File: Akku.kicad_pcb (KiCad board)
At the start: 2 copper layers, 100 x 160 mm, 46 parts, among them J1 +/- Stecker, J2 load/up, J3 down/en/clear, P7 CONN_02X10, P8 CONN_02X10, P9 CONN_02X10, SW1 UP_Bonsai_SWITCH_INV, SW2 DOWN_Bonsai_SWITCH_INV, SW3 CLR_Bonsai_SWITCH_INV, U1 74HC14, U2 7400, U4 7408, U5 74LS193, U6 74LS541, U7 74LS193, U8 74LS540

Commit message: akku and wireing in pcb
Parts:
- moved D3 74.6 mm to (117.5, 170.8)
- moved D1 65.1 mm to (63.5, 119.4), turned to 180 degrees
- moved U5 34.9 mm to (107.3, 171.4)
- moved U7 13.4 mm to (83.2, 171.4)
- moved D4 12.7 mm to (94.0, 121.9)
- moved R13 12.7 mm to (94.0, 124.5)
- moved D5 11.4 mm to (99.1, 121.9)
- moved R15 11.4 mm to (99.1, 124.7)
- moved D2 10.9 mm to (114.9, 177.8)
- moved U8 10.2 mm to (99.1, 149.9)
- moved D6 10.2 mm to (104.1, 121.9)
- moved R16 10.2 mm to (104.1, 124.7)
- moved D8 8.89 mm to (109.2, 121.9)
- moved R17 8.89 mm to (109.2, 124.7)
- moved D9 7.62 mm to (114.3, 121.9)
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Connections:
- SW3 pad 6: (no net) -> GND
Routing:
- net GND: track 255.3 -> 592.3 mm, vias 2 -> 8
- net Net-(U1-Pad4): track 2.54 -> 209.1 mm
- net VCC: track 595.8 -> 780.3 mm, vias 0 -> 4
- net Net-(D7-Pad2): track 0.00 -> 144.8 mm
- net Net-(D1-Pad2): track 0.00 -> 122.4 mm
- net CLR: track 27.2 -> 125.1 mm, vias 0 -> 3
- net Net-(U1-Pad11): track 0.00 -> 95.3 mm, vias 0 -> 1
- net Net-(U1-Pad13): track 28.6 -> 107.7 mm, vias 0 -> 1
- net RPB4: track 45.9 -> 116.1 mm, vias 0 -> 4
- net RPB3: track 21.9 -> 82.8 mm, vias 0 -> 2
- net Net-(D2-Pad2): track 0.00 -> 30.6 mm
- net Net-(D3-Pad2): track 0.00 -> 26.3 mm
- net Net-(R12-Pad2): track 14.4 -> 21.4 mm
- net ^enable: track 108.0 -> 111.0 mm
- net Net-(R9-Pad2): track 17.4 -> 20.0 mm
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
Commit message: Akku pc finished
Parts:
- added C1: C, tg_foodprint:C_Disc_D10.0mm_W2.5mm_P5.00mm, F.Cu at (86.4, 172.7)
- added C2: C, tg_foodprint:C_Disc_D10.0mm_W2.5mm_P5.00mm, F.Cu at (66.7, 208.9)
- added C3: C, tg_foodprint:C_Disc_D10.0mm_W2.5mm_P5.00mm, F.Cu at (94.0, 149.9)
- added D13: D, Pin_Headers:D_DO-41_SOD81_P10.16mm_Horizontal, F.Cu at (63.5, 87.6)
- moved U7 24.3 mm to (107.4, 171.4)
- moved U5 24.1 mm to (83.2, 171.3)
- moved P7 1.27 mm to (48.3, 113.0)
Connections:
- U5 pad 12: Net-(U5-Pad12) -> (no net)
- U5 pad 13: Net-(U5-Pad13) -> (no net)
- U5 pad 4: Net-(U1-Pad13) -> Net-(U5-Pad4)
- U5 pad 5: Net-(U1-Pad11) -> Net-(U5-Pad5)
- U7 pad 12: (no net) -> Net-(U5-Pad5)
- U7 pad 13: (no net) -> Net-(U5-Pad4)
- U7 pad 4: Net-(U5-Pad13) -> Net-(U1-Pad13)
- U7 pad 5: Net-(U5-Pad12) -> Net-(U1-Pad11)
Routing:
- net /a7: track 0.00 -> 303.7 mm, vias 0 -> 4
- net /a6: track 0.00 -> 302.3 mm, vias 0 -> 6
- net /a5: track 0.00 -> 272.5 mm, vias 0 -> 6
- net /a2: track 0.00 -> 268.1 mm, vias 0 -> 6
- net /a4: track 0.00 -> 262.0 mm, vias 0 -> 6
- net /a3: track 0.00 -> 246.2 mm, vias 0 -> 6
- net /a1: track 0.00 -> 215.7 mm, vias 0 -> 6
- net /a0: track 0.00 -> 204.4 mm, vias 0 -> 4
- net Net-(U6-Pad8): track 0.00 -> 80.4 mm, vias 0 -> 2
- net Net-(U6-Pad6): track 0.00 -> 69.9 mm, vias 0 -> 2
- net Net-(U6-Pad7): track 0.00 -> 69.9 mm, vias 0 -> 2
- net Net-(U5-Pad3): track 0.00 -> 67.8 mm, vias 0 -> 2
- net Net-(U6-Pad9): track 0.00 -> 66.9 mm
- net Net-(U5-Pad2): track 0.00 -> 61.1 mm, vias 0 -> 2
- net GND: track 592.3 -> 652.5 mm, vias 8 -> 11
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
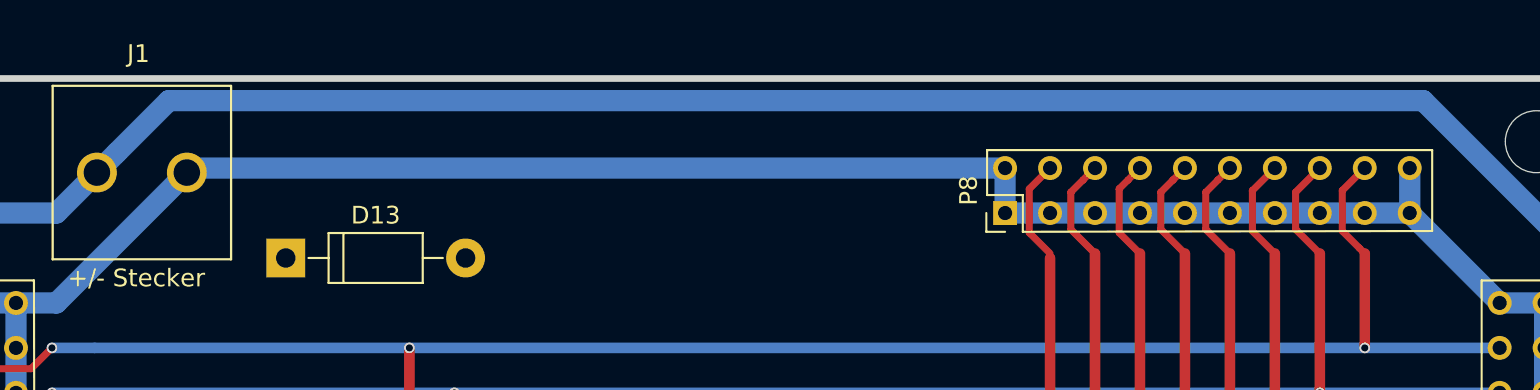
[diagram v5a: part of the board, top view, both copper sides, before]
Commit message: Eintakt libs fixed
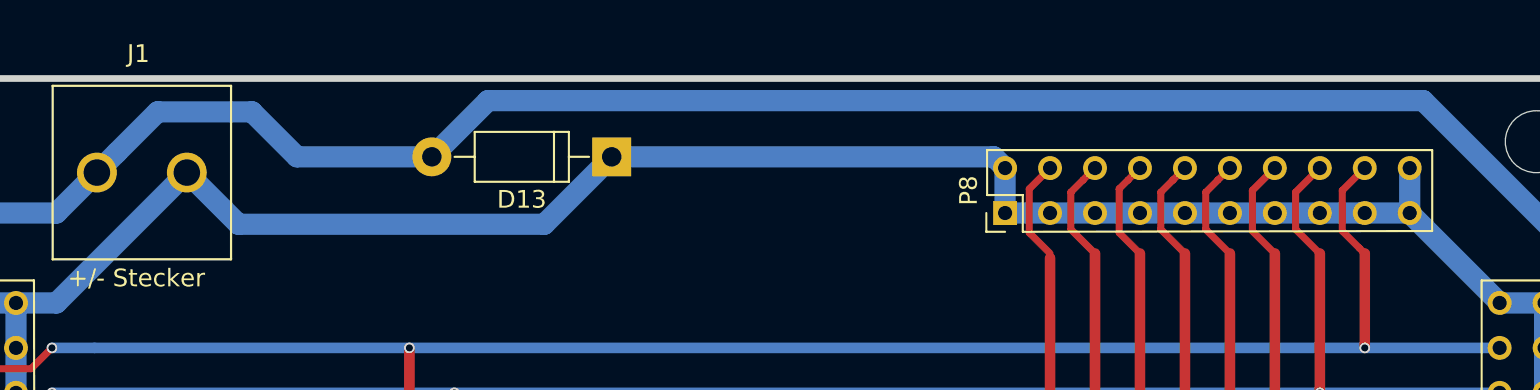
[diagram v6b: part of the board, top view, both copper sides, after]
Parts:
- moved D13 19.3 mm to (81.9, 81.9), turned to 180 degrees
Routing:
- net GND: track 652.5 -> 655.5 mm
- net VCC: track 785.1 -> 787.2 mm
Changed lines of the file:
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@@
     (thickness 1.6)
     (drawings 3)
-    (tracks 850)
+    (tracks 857)
     (zones 0)
     (modules 50)
@@
     (visible_elements FFFFFF7F)
     (pcbplotparams
-      (layerselection 0x00030_80000001)
+      (layerselection 0x00030_ffffffff)
       (usegerberextensions false)
       (usegerberattributes false)
       (usegerberadvancedattributes false)
       (creategerberjobfile false)
-      (excludeedgelayer true)
+      (excludeedgelayer false)
       (linewidth 0.100000)
       (plotframeref false)
@@
       (padsonsilk false)
       (subtractmaskfromsilk false)
-      (outputformat 1)
+      (outputformat 4)
       (mirror false)
-      (drillshape 1)
+      (drillshape 0)
       (scaleselection 1)
       (outputdirectory ""))
@@
   )
   (module Pin_Headers:D_DO-41_SOD81_P10.16mm_Horizontal (layer F.Cu)
-    (at 63.5 87.63)
+    (at 81.915 81.915 180)
     (descr "D, DO-41_SOD81 series, Axial, Horizontal, pin pitch=10.16mm, , length*diameter=5.2*2.7mm^2, , http://www.diodes.com/_files/packages/DO-41%20(Plastic).pdf")
     (tags "D DO-41_SOD81 series Axial Horizontal pin pitch 10.16mm  length 5.2mm diameter 2.7mm")
-    (fp_text reference D13 (at 5.08 -2.41) (layer F.SilkS)
-      (effects (font (size 1 1) (thickness 0.15)))
-    )
-    (fp_text value D (at 5.08 2.41) (layer F.Fab)
+    (fp_text reference D13 (at 5.08 -2.41 180) (layer F.SilkS)
+      (effects (font (size 1 1) (thickness 0.15)))
+    )
+    (fp_text value D (at 5.08 2.41 180) (layer F.Fab)
       (effects (font (size 1 1) (thickness 0.15)))
     )
@@
     (fp_line (start 2.48 1.35) (end 7.68 1.35) (layer F.Fab) (width 0.1))
     (fp_line (start 2.48 -1.35) (end 2.48 1.35) (layer F.Fab) (width 0.1))
-    (fp_text user %R (at 5.08 0) (layer F.Fab)
-      (effects (font (size 1 1) (thickness 0.15)))
-    )
-    (pad 2 thru_hole oval (at 10.16 0) (size 2.2 2.2) (drill 1.1) (layers *.Cu *.Mask)
+    (fp_text user %R (at 5.08 0 180) (layer F.Fab)
+      (effects (font (size 1 1) (thickness 0.15)))
+    )
+    (pad 2 thru_hole oval (at 10.16 0 180) (size 2.2 2.2) (drill 1.1) (layers *.Cu *.Mask)
       (net 2 VCC))
-    (pad 1 thru_hole rect (at 0 0) (size 2.2 2.2) (drill 1.1) (layers *.Cu *.Mask)
+    (pad 1 thru_hole rect (at 0 0 180) (size 2.2 2.2) (drill 1.1) (layers *.Cu *.Mask)
       (net 10 GND))
     (model ${KISYS3DMOD}/Diodes_THT.3dshapes/D_DO-41_SOD81_P10.16mm_Horizontal.wrl
@@
   (segment (start 82.55 224.155) (end 82.55 219.075) (width 1.2) (layer B.Cu) (net 2))
   (segment (start 83.82 206.745823) (end 83.82 205.74) (width 0.6) (layer B.Cu) (net 2))
-  (segment (start 53.956999 81.679001) (end 52.832 82.804) (width 1.2) (layer B.Cu) (net 2) (status 20))
-  (segment (start 138.60999 89.589992) (end 127.759998 78.74) (width 1.2) (layer B.Cu) (net 2))
-  (segment (start 127.759998 78.74) (end 56.896 78.74) (width 1.2) (layer B.Cu) (net 2))
   (segment (start 82.55 231.14) (end 100.33 231.14) (width 1.2) (layer B.Cu) (net 2))
   (segment (start 105.41 236.22) (end 127 236.22) (width 1.2) (layer B.Cu) (net 2))
   (segment (start 137.130001 231.169999) (end 138.60999 229.69001) (width 1.2) (layer B.Cu) (net 2))
   (segment (start 127 236.22) (end 132.050001 231.169999) (width 1.2) (layer B.Cu) (net 2))
-  (segment (start 56.896 78.74) (end 53.956999 81.679001) (width 1.2) (layer B.Cu) (net 2))
   (segment (start 100.33 231.14) (end 105.41 236.22) (width 1.2) (layer B.Cu) (net 2))
   (segment (start 132.050001 231.169999) (end 137.130001 231.169999) (width 1.2) (layer B.Cu) (net 2))
@@
   (segment (start 52.832 82.804) (end 50.546 85.09) (width 1.2) (layer B.Cu) (net 2) (status 10))
   (segment (start 138.60999 119.38) (end 93.98 119.38) (width 1.2) (layer B.Cu) (net 2) (status 20))
-  (segment (start 138.60999 119.38) (end 138.60999 89.589992) (width 1.2) (layer B.Cu) (net 2))
   (segment (start 138.60999 229.69001) (end 138.60999 119.38) (width 1.2) (layer B.Cu) (net 2))
   (segment (start 66.675 144.78) (end 65.405 143.51) (width 1.2) (layer B.Cu) (net 2))
@@
   (segment (start 69.135 203.915) (end 69.85 203.2) (width 1.2) (layer B.Cu) (net 2))
   (segment (start 66.675 203.915) (end 69.135 203.915) (width 1.2) (layer B.Cu) (net 2))
+  (segment (start 53.956999 81.679001) (end 52.832 82.804) (width 1.2) (layer B.Cu) (net 2))
+  (segment (start 61.595 79.375) (end 56.261 79.375) (width 1.2) (layer B.Cu) (net 2))
+  (segment (start 138.60999 89.589992) (end 127.759998 78.74) (width 1.2) (layer B.Cu) (net 2))
+  (segment (start 127.759998 78.74) (end 74.93 78.74) (width 1.2) (layer B.Cu) (net 2))
+  (segment (start 74.93 78.74) (end 71.755 81.915) (width 1.2) (layer B.Cu) (net 2))
+  (segment (start 138.60999 119.38) (end 138.60999 89.589992) (width 1.2) (layer B.Cu) (net 2))
+  (segment (start 71.755 81.915) (end 64.135 81.915) (width 1.2) (layer B.Cu) (net 2))
+  (segment (start 56.261 79.375) (end 53.956999 81.679001) (width 1.2) (layer B.Cu) (net 2))
+  (segment (start 64.135 81.915) (end 61.595 79.375) (width 1.2) (layer B.Cu) (net 2))
   (segment (start 99.06 121.92) (end 99.06 124.714) (width 0.6) (layer B.Cu) (net 3) (status 30))
   (segment (start 104.14 124.714) (end 104.14 121.92) (width 0.6) (layer B.Cu) (net 4) (status 30))
@@
   (segment (start 48.006 228.346) (end 43.18 223.52) (width 1.2) (layer B.Cu) (net 10))
   (segment (start 64.77 228.346) (end 58.42 228.346) (width 1.2) (layer B.Cu) (net 10) (status 30))
-  (segment (start 58.166 82.55) (end 57.912 82.804) (width 1.2) (layer B.Cu) (net 10) (status 30))
-  (segment (start 104.14 82.55) (end 58.166 82.55) (width 1.2) (layer B.Cu) (net 10) (status 30))
   (segment (start 104.14 82.55) (end 104.14 85.09) (width 1.2) (layer B.Cu) (net 10) (status 30))
   (segment (start 124.251002 85.09) (end 127 85.09) (width 1.2) (layer B.Cu) (net 10) (status 30))
@@
   (segment (start 64.77 210.82) (end 66.675 208.915) (width 1.2) (layer B.Cu) (net 10))
   (segment (start 63.5 210.82) (end 64.77 210.82) (width 1.2) (layer B.Cu) (net 10))
+  (segment (start 78.105 85.725) (end 60.833 85.725) (width 1.2) (layer B.Cu) (net 10))
+  (segment (start 81.915 81.915) (end 78.105 85.725) (width 1.2) (layer B.Cu) (net 10))
+  (segment (start 104.14 82.55) (end 103.505 81.915) (width 1.2) (layer B.Cu) (net 10))
+  (segment (start 60.833 85.725) (end 57.912 82.804) (width 1.2) (layer B.Cu) (net 10))
+  (segment (start 103.505 81.915) (end 81.915 81.915) (width 1.2) (layer B.Cu) (net 10))
   (segment (start 96.52 203.2) (end 96.52 200.66) (width 1.2) (layer B.Cu) (net 11) (status 30))
   (segment (start 46.355 133.985) (end 60.96 119.38) (width 0.6) (layer B.Cu) (net 12) (status 20))

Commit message: BIB Cleanup finished
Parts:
- C1, C2, C3: footprint tg_foodprint:C_Disc_D10.0mm_W2.5mm_P5.00mm -> allBonsaiFootprintsLibs:C_Disc_D10.0mm_W2.5mm_P5.00mm
- P7, P8, P9: footprint tg_foodprint:Pin_Header_Straight_2x10_Pitch2.00mmBonsai.pretty -> allBonsaiFootprintsLibs:Pin_Header_Straight_2x10_Pitch2.00mmBonsai.pretty
- REF**: footprint tg_foodprint:EuroBoard160mmX100mm_holes -> allBonsaiFootprintsLibs:EuroBoard160mmX100mm_holes
- SW1, SW2, SW3: footprint tg_foodprint:SW_PUSH_LCD_E3_SAxxxx_tg_V2 -> allBonsaiFootprintsLibs:SW_PUSH_LCD_E3_SAxxxx_tg_V2
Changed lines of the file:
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@@
-(kicad_pcb (version 20171130) (host pcbnew 6.0.0-rc1-unknown-dffa399~84~ubuntu18.04.1)
+(kicad_pcb (version 20171130) (host pcbnew 5.1.0-rc1-unknown-c0a86d7~84~ubuntu18.04.1)
   (general
     (thickness 1.6)
@@
   )
   (page A4 portrait)
+  (title_block
+    (title Akku/PC)
+    (date 2019-02-11)
+    (company AGI)
+  )
   (layers
     (0 F.Cu signal)
@@
     )
   )
-  (module tg_foodprint:Pin_Header_Straight_2x10_Pitch2.00mmBonsai.pretty (layer F.Cu)
+  (module allBonsaiFootprintsLibs:Pin_Header_Straight_2x10_Pitch2.00mmBonsai.pretty (layer F.Cu)
     (at 48.26 113.03 180)
     (descr "Through hole straight pin header, 2x10, 2.00mm pitch, double rows")
@@
     )
   )
-  (module tg_foodprint:Pin_Header_Straight_2x10_Pitch2.00mmBonsai.pretty (layer F.Cu)
+  (module allBonsaiFootprintsLibs:Pin_Header_Straight_2x10_Pitch2.00mmBonsai.pretty (layer F.Cu)
     (at 104.14 85.09 90)
     (descr "Through hole straight pin header, 2x10, 2.00mm pitch, double rows")
@@
     )
   )
-  (module tg_foodprint:Pin_Header_Straight_2x10_Pitch2.00mmBonsai.pretty (layer F.Cu)
+  (module allBonsaiFootprintsLibs:Pin_Header_Straight_2x10_Pitch2.00mmBonsai.pretty (layer F.Cu)
     (at 134.62 113.03 180)
     (descr "Through hole straight pin header, 2x10, 2.00mm pitch, double rows")
@@
       (net 60 CLR))
   )
-  (module tg_foodprint:SW_PUSH_LCD_E3_SAxxxx_tg_V2 (layer F.Cu)
+  (module allBonsaiFootprintsLibs:SW_PUSH_LCD_E3_SAxxxx_tg_V2 (layer F.Cu)
     (at 58.42 228.346 270)
     (descr "Switch with LCD screen E3 SAxxxx")
@@
     )
   )
-  (module tg_foodprint:SW_PUSH_LCD_E3_SAxxxx_tg_V2 (layer F.Cu)
+  (module allBonsaiFootprintsLibs:SW_PUSH_LCD_E3_SAxxxx_tg_V2 (layer F.Cu)
     (at 72.39 228.346 270)
     (descr "Switch with LCD screen E3 SAxxxx")
@@
     )
   )
-  (module tg_foodprint:SW_PUSH_LCD_E3_SAxxxx_tg_V2 (layer F.Cu)
+  (module allBonsaiFootprintsLibs:SW_PUSH_LCD_E3_SAxxxx_tg_V2 (layer F.Cu)
     (at 86.36 228.346 270)
     (descr "Switch with LCD screen E3 SAxxxx")
@@
       (net 49 RPB4))
   )
-  (module tg_foodprint:EuroBoard160mmX100mm_holes (layer F.Cu)
+  (module allBonsaiFootprintsLibs:EuroBoard160mmX100mm_holes (layer F.Cu)
     (at 139.7 237.49 90)
     (descr "Outline, Eurocard, 100x160mm, with holes 3,5mm,")
@@
     (pad "" np_thru_hole circle (at 3.57 -5.55 90) (size 3.5 3.5) (drill 3.5) (layers *.Cu *.Mask))
   )
-  (module tg_foodprint:C_Disc_D10.0mm_W2.5mm_P5.00mm (layer F.Cu)
+  (module allBonsaiFootprintsLibs:C_Disc_D10.0mm_W2.5mm_P5.00mm (layer F.Cu)
     (at 86.36 172.72 270)
     (descr "C, Disc series, Radial, pin pitch=5.00mm, , diameter*width=10*2.5mm^2, Capacitor, http://cdn-reichelt.de/documents/datenblatt/B300/DS_KERKO_TC.pdf")
@@
     )
   )
-  (module tg_foodprint:C_Disc_D10.0mm_W2.5mm_P5.00mm (layer F.Cu)
+  (module allBonsaiFootprintsLibs:C_Disc_D10.0mm_W2.5mm_P5.00mm (layer F.Cu)
     (at 66.675 208.915 90)
     (descr "C, Disc series, Radial, pin pitch=5.00mm, , diameter*width=10*2.5mm^2, Capacitor, http://cdn-reichelt.de/documents/datenblatt/B300/DS_KERKO_TC.pdf")
@@
     )
   )
-  (module tg_foodprint:C_Disc_D10.0mm_W2.5mm_P5.00mm (layer F.Cu)
+  (module allBonsaiFootprintsLibs:C_Disc_D10.0mm_W2.5mm_P5.00mm (layer F.Cu)
     (at 93.98 149.86 90)
     (descr "C, Disc series, Radial, pin pitch=5.00mm, , diameter*width=10*2.5mm^2, Capacitor, http://cdn-reichelt.de/documents/datenblatt/B300/DS_KERKO_TC.pdf")
@@
   (segment (start 93.98 119.38) (end 92.075 119.38) (width 1.2) (layer B.Cu) (net 2) (status 10))
   (segment (start 92.075 119.38) (end 90.805 120.65) (width 1.2) (layer B.Cu) (net 2))
-  (segment (start 90.805 144.78) (end 94.615 144.78) (width 1.2) (layer B.Cu) (net 2))
-  (segment (start 94.615 144.78) (end 96.52 142.875) (width 1.2) (layer B.Cu) (net 2))
+  (segment (start 90.805 144.78) (end 94.615 144.78) (width 1.2) (layer B.Cu) (net 2) (status 20))
+  (segment (start 94.615 144.78) (end 96.52 142.875) (width 1.2) (layer B.Cu) (net 2) (status 10))
   (segment (start 97.06 142.24) (end 99.06 142.24) (width 1.2) (layer B.Cu) (net 2) (status 20))
   (segment (start 96.52 142.78) (end 97.06 142.24) (width 1.2) (layer B.Cu) (net 2))
@@
   (segment (start 81.28 210.48998) (end 81.28 208.28) (width 0.3) (layer B.Cu) (net 2))
   (segment (start 78.74 208.28) (end 78.74 214.63) (width 0.3) (layer B.Cu) (net 2))
-  (segment (start 85.137 178.943) (end 86.36 177.72) (width 1.2) (layer B.Cu) (net 2))
-  (segment (start 83.185 178.943) (end 85.137 178.943) (width 1.2) (layer B.Cu) (net 2))
+  (segment (start 85.137 178.943) (end 86.36 177.72) (width 1.2) (layer B.Cu) (net 2) (status 20))
+  (segment (start 83.185 178.943) (end 85.137 178.943) (width 1.2) (layer B.Cu) (net 2) (status 10))
   (segment (start 68.58 214.63) (end 78.74 214.63) (width 0.6) (layer B.Cu) (net 2))
   (segment (start 67.31 213.36) (end 68.58 214.63) (width 0.6) (layer B.Cu) (net 2))
@@
   (segment (start 68.449999 209.139999) (end 68.449999 209.680001) (width 0.6) (layer B.Cu) (net 2))
   (segment (start 69.85 207.645) (end 68.58 208.915) (width 0.6) (layer B.Cu) (net 2))
-  (segment (start 69.85 203.2) (end 69.85 207.645) (width 0.6) (layer B.Cu) (net 2))
+  (segment (start 69.85 203.2) (end 69.85 207.645) (width 0.6) (layer B.Cu) (net 2) (status 10))
   (segment (start 68.58 208.915) (end 68.58 209.019999) (width 0.6) (layer B.Cu) (net 2))
   (segment (start 67.31 210.82) (end 67.31 213.36) (width 0.6) (layer B.Cu) (net 2))
   (segment (start 68.58 209.019999) (end 68.569999 209.019999) (width 0.6) (layer B.Cu) (net 2))
   (segment (start 68.569999 209.019999) (end 68.449999 209.139999) (width 0.6) (layer B.Cu) (net 2))
-  (segment (start 69.135 203.915) (end 69.85 203.2) (width 1.2) (layer B.Cu) (net 2))
-  (segment (start 66.675 203.915) (end 69.135 203.915) (width 1.2) (layer B.Cu) (net 2))
-  (segment (start 53.956999 81.679001) (end 52.832 82.804) (width 1.2) (layer B.Cu) (net 2))
+  (segment (start 69.135 203.915) (end 69.85 203.2) (width 1.2) (layer B.Cu) (net 2) (status 30))
+  (segment (start 66.675 203.915) (end 69.135 203.915) (width 1.2) (layer B.Cu) (net 2) (status 30))
+  (segment (start 53.956999 81.679001) (end 52.832 82.804) (width 1.2) (layer B.Cu) (net 2) (status 20))
   (segment (start 61.595 79.375) (end 56.261 79.375) (width 1.2) (layer B.Cu) (net 2))
   (segment (start 138.60999 89.589992) (end 127.759998 78.74) (width 1.2) (layer B.Cu) (net 2))
   (segment (start 127.759998 78.74) (end 74.93 78.74) (width 1.2) (layer B.Cu) (net 2))
-  (segment (start 74.93 78.74) (end 71.755 81.915) (width 1.2) (layer B.Cu) (net 2))
+  (segment (start 74.93 78.74) (end 71.755 81.915) (width 1.2) (layer B.Cu) (net 2) (status 20))
   (segment (start 138.60999 119.38) (end 138.60999 89.589992) (width 1.2) (layer B.Cu) (net 2))
-  (segment (start 71.755 81.915) (end 64.135 81.915) (width 1.2) (layer B.Cu) (net 2))
+  (segment (start 71.755 81.915) (end 64.135 81.915) (width 1.2) (layer B.Cu) (net 2) (status 10))
   (segment (start 56.261 79.375) (end 53.956999 81.679001) (width 1.2) (layer B.Cu) (net 2))
   (segment (start 64.135 81.915) (end 61.595 79.375) (width 1.2) (layer B.Cu) (net 2))
@@
   (segment (start 48.26 114.3) (end 48.26 113.03) (width 1.2) (layer B.Cu) (net 10) (status 20))
   (segment (start 48.26 113.03) (end 45.72 113.03) (width 1.2) (layer B.Cu) (net 10) (status 30))
-  (segment (start 87.63 171.45) (end 86.36 172.72) (width 1.2) (layer B.Cu) (net 10))
-  (segment (start 89.662 171.45) (end 87.63 171.45) (width 1.2) (layer B.Cu) (net 10))
-  (segment (start 64.77 210.82) (end 66.675 208.915) (width 1.2) (layer B.Cu) (net 10))
-  (segment (start 63.5 210.82) (end 64.77 210.82) (width 1.2) (layer B.Cu) (net 10))
+  (segment (start 87.63 171.45) (end 86.36 172.72) (width 1.2) (layer B.Cu) (net 10) (status 20))
+  (segment (start 89.662 171.45) (end 87.63 171.45) (width 1.2) (layer B.Cu) (net 10) (status 10))
+  (segment (start 64.77 210.82) (end 66.675 208.915) (width 1.2) (layer B.Cu) (net 10) (status 20))
+  (segment (start 63.5 210.82) (end 64.77 210.82) (width 1.2) (layer B.Cu) (net 10) (status 10))
   (segment (start 78.105 85.725) (end 60.833 85.725) (width 1.2) (layer B.Cu) (net 10))
-  (segment (start 81.915 81.915) (end 78.105 85.725) (width 1.2) (layer B.Cu) (net 10))
-  (segment (start 104.14 82.55) (end 103.505 81.915) (width 1.2) (layer B.Cu) (net 10))
-  (segment (start 60.833 85.725) (end 57.912 82.804) (width 1.2) (layer B.Cu) (net 10))
-  (segment (start 103.505 81.915) (end 81.915 81.915) (width 1.2) (layer B.Cu) (net 10))
+  (segment (start 81.915 81.915) (end 78.105 85.725) (width 1.2) (layer B.Cu) (net 10) (status 10))
+  (segment (start 104.14 82.55) (end 103.505 81.915) (width 1.2) (layer B.Cu) (net 10) (status 30))
+  (segment (start 60.833 85.725) (end 57.912 82.804) (width 1.2) (layer B.Cu) (net 10) (status 20))
+  (segment (start 103.505 81.915) (end 81.915 81.915) (width 1.2) (layer B.Cu) (net 10) (status 30))
   (segment (start 96.52 203.2) (end 96.52 200.66) (width 1.2) (layer B.Cu) (net 11) (status 30))
   (segment (start 46.355 133.985) (end 60.96 119.38) (width 0.6) (layer B.Cu) (net 12) (status 20))
@@
   (segment (start 69.088 128.27) (end 88.265 128.27) (width 0.6) (layer F.Cu) (net 44))
   (via (at 88.265 128.27) (size 0.6) (drill 0.4) (layers F.Cu B.Cu) (net 44))
-  (segment (start 104.775 184.15) (end 104.775 179.07) (width 0.6) (layer B.Cu) (net 44))
+  (segment (start 104.775 184.15) (end 104.775 179.07) (width 0.6) (layer B.Cu) (net 44) (status 20))
   (segment (start 99.06 184.15) (end 104.775 184.15) (width 0.6) (layer B.Cu) (net 44))
   (segment (start 55.626 128.27) (end 49.784 134.112) (width 0.6) (layer B.Cu) (net 44))
